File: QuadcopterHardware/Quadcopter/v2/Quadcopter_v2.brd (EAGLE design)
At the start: 47 x 28 mm, 43 parts, among them J1 FTDI_DEVICE, M1 WIRELESS-NRF24L01, U1 ATMEGA328P_TQFP, U3 GY-521MPU6050

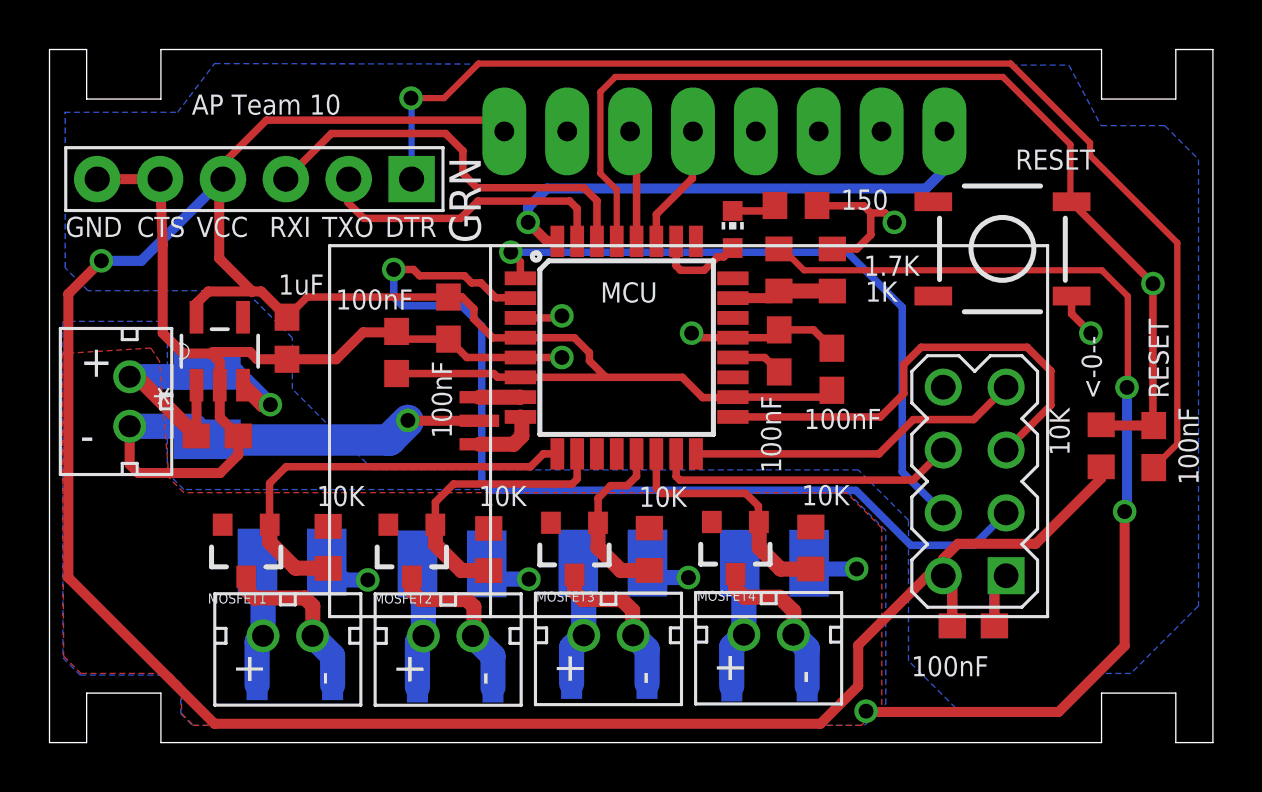
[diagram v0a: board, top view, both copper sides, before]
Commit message: moved ground pour
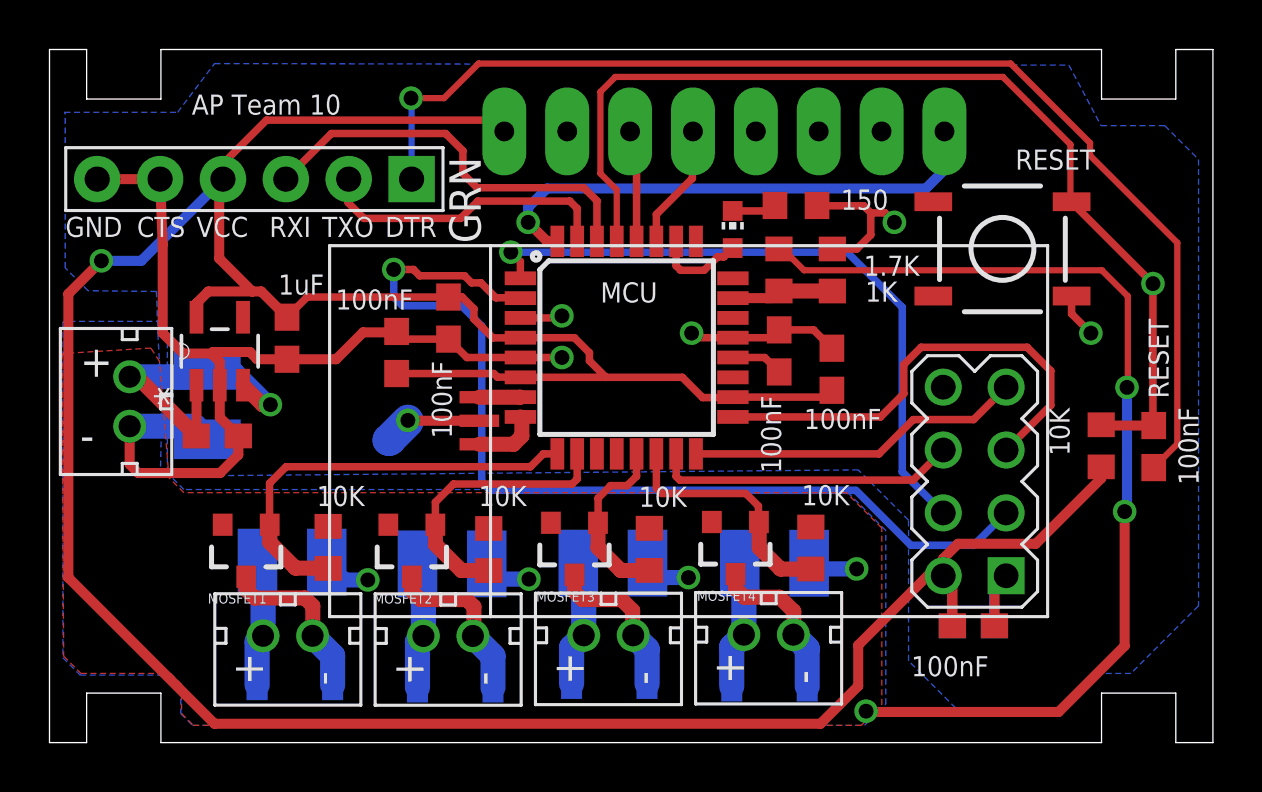
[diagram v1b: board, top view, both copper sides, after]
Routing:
- net GND: track 80.6 -> 73.7 mm
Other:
- board text removed: "<-0--"
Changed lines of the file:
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@@
 <?xml version="1.0" encoding="utf-8"?>
 <!DOCTYPE eagle SYSTEM "eagle.dtd">
-<eagle version="7.7.0">
+<eagle version="8.0.1">
 <drawing>
 <settings>
@@
 <text x="46.4185" y="10.414" size="0.8128" layer="21" rot="R90">100nF</text>
 <text x="45.212" y="13.9065" size="0.8128" layer="21" rot="R90">RESET</text>
-<text x="42.51325" y="13.87475" size="0.8128" layer="21" rot="R90">&lt;-0--</text>
 <text x="31.97225" y="21.5265" size="0.8128" layer="21">150</text>
 <text x="32.9565" y="17.81175" size="0.8128" layer="21">1K</text>
@@
 <wire x1="38.64575" y1="6.74025" x2="38.16925" y2="6.26375" width="0.4064" layer="16"/>
 <wire x1="38.16925" y1="6.26375" x2="38.16925" y2="4.71825" width="0.4064" layer="16"/>
-<polygon width="0.3048" layer="16" isolate="0.3048">
+<polygon width="0.3048" layer="16" isolate="0.3048" rank="2">
 <vertex x="0.60325" y="25.4635"/>
 <vertex x="5.17525" y="25.4635"/>
@@
 <vertex x="34.70275" y="8.98525"/>
 <vertex x="32.67075" y="11.01725"/>
-<vertex x="13.081" y="11.01725"/>
-<vertex x="9.81075" y="14.2875"/>
-<vertex x="9.81075" y="16.35125"/>
-<vertex x="7.90575" y="18.25625"/>
+<vertex x="4.47675" y="10.76325"/>
+<vertex x="4.54025" y="13.55725"/>
+<vertex x="4.3815" y="16.4465"/>
+<vertex x="4.318" y="18.2245"/>
 <vertex x="1.55575" y="18.25625"/>
 <vertex x="0.635" y="19.177"/>
@@
 <via x="14.478" y="13.0175" extent="1-16" drill="0.6"/>
 <wire x1="14.478" y1="13.0175" x2="13.68425" y2="12.22375" width="1.27" layer="16"/>
-<wire x1="13.68425" y1="12.22375" x2="6.858" y2="12.22375" width="1.27" layer="16"/>
 <wire x1="13.68425" y1="12.22375" x2="13.74775" y2="12.22375" width="1.27" layer="16"/>
 <wire x1="13.74775" y1="12.22375" x2="14.478" y2="12.954" width="1.27" layer="16"/>
